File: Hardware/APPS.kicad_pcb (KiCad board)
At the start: 2 copper layers, 104.1 x 63 mm, 86 parts, among them J1 Screw_Terminal_01x02, J2 Screw_Terminal_01x03, J3 Screw_Terminal_01x03, J4 Conn_01x06_Male, J5 Screw_Terminal_01x02, J6 Conn_01x06_Male, J7 Screw_Terminal_01x02, K1 FINDER-30.22, Q1 BSS138, SW1 SW_Push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

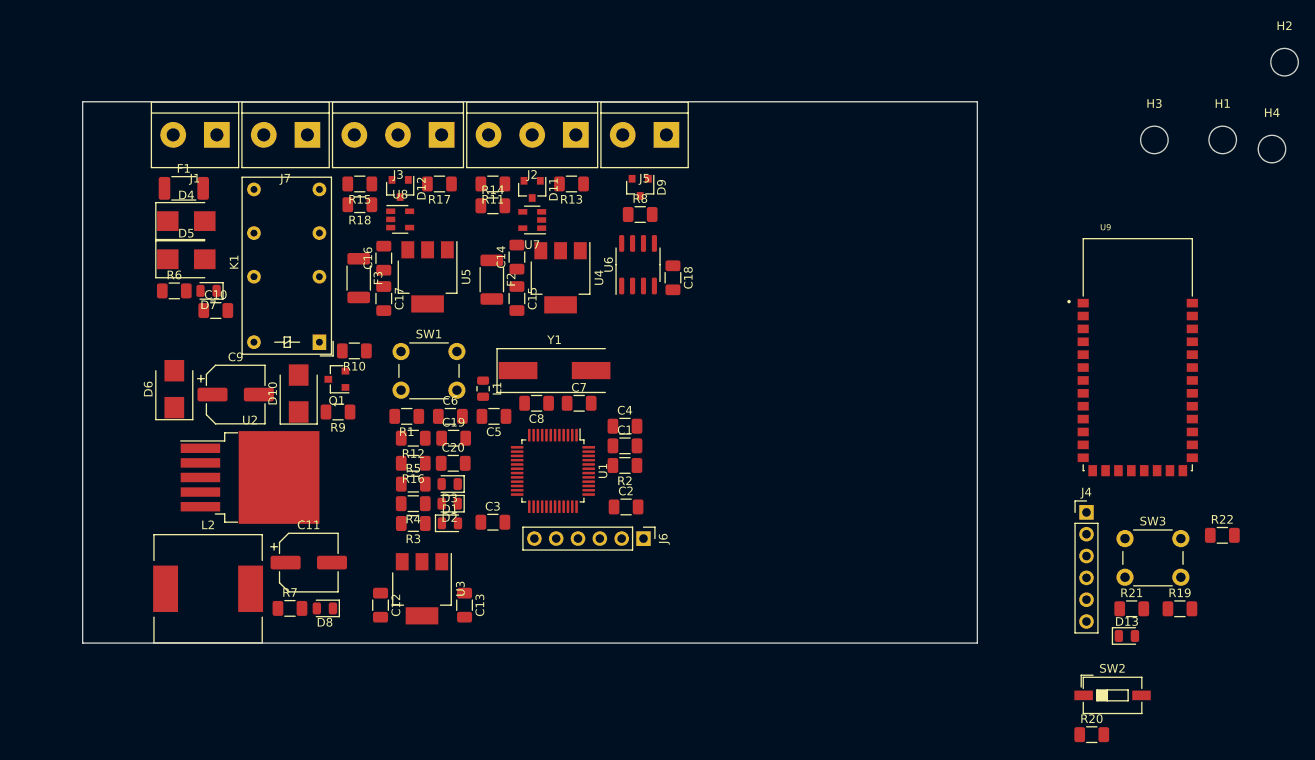
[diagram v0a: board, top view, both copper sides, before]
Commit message: Changed PCB edhes shape
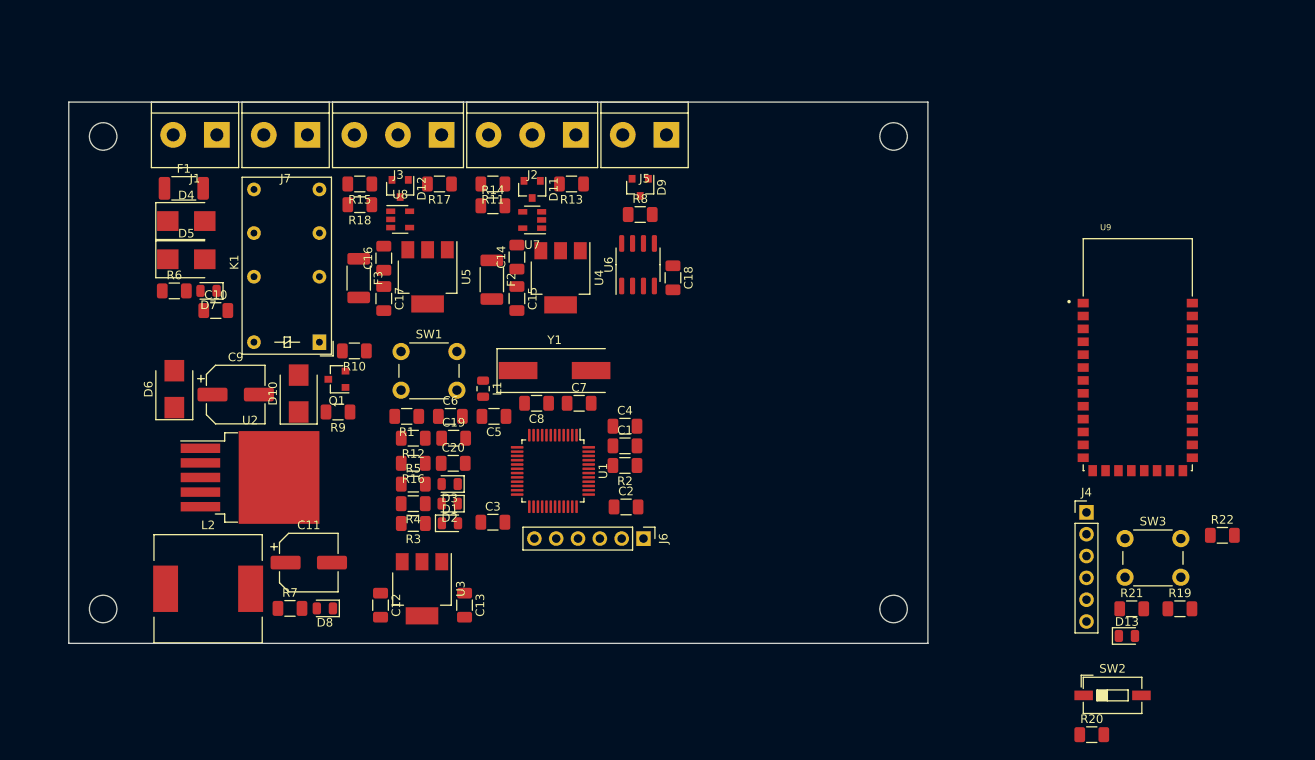
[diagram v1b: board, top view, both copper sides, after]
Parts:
- removed H1, H2, H3, H4: MountingHole, MountingHole:MountingHole_3.2mm_M3
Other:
- board size 104.1 x 63 mm -> 100 x 63 mm
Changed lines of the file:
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@@
   (general
     (thickness 1.6)
-    (drawings 4)
+    (drawings 8)
     (tracks 0)
     (zones 0)
-    (modules 86)
+    (modules 82)
     (nets 108)
   )
@@
     (solder_mask_min_width 0.25)
     (aux_axis_origin 0 0)
-    (visible_elements FFFFFF7F)
+    (visible_elements 7FFFFFFF)
     (pcbplotparams
       (layerselection 0x010fc_ffffffff)
@@
     )
   )
-  (module MountingHole:MountingHole_3.2mm_M3 (layer F.Cu)
-    (at 206.354001 56.975001)
-    (descr "Mounting Hole 3.2mm, no annular, M3")
-    (tags "mounting hole 3.2mm no annular m3")
-    (attr virtual)
-    (fp_text reference H1 (at 0 -4.2) (layer F.SilkS)
-      (effects (font (size 1 1) (thickness 0.15)))
-    )
-    (fp_text value MountingHole (at 0 4.2) (layer F.Fab)
-      (effects (font (size 1 1) (thickness 0.15)))
-    )
-    (fp_text user %R (at 0.3 0) (layer F.Fab)
-      (effects (font (size 1 1) (thickness 0.15)))
-    )
-    (fp_circle (center 0 0) (end 3.2 0) (layer Cmts.User) (width 0.15))
-    (fp_circle (center 0 0) (end 3.45 0) (layer F.CrtYd) (width 0.05))
-    (pad 1 np_thru_hole circle (at 0 0) (size 3.2 3.2) (drill 3.2) (layers *.Cu *.Mask))
-  )
-  (module MountingHole:MountingHole_3.2mm_M3 (layer F.Cu)
-    (at 213.554001 47.925001)
-    (descr "Mounting Hole 3.2mm, no annular, M3")
-    (tags "mounting hole 3.2mm no annular m3")
-    (attr virtual)
-    (fp_text reference H2 (at 0 -4.2) (layer F.SilkS)
-      (effects (font (size 1 1) (thickness 0.15)))
-    )
-    (fp_text value MountingHole (at 0 4.2) (layer F.Fab)
-      (effects (font (size 1 1) (thickness 0.15)))
-    )
-    (fp_circle (center 0 0) (end 3.45 0) (layer F.CrtYd) (width 0.05))
-    (fp_circle (center 0 0) (end 3.2 0) (layer Cmts.User) (width 0.15))
-    (fp_text user %R (at 0.3 0) (layer F.Fab)
-      (effects (font (size 1 1) (thickness 0.15)))
-    )
-    (pad 1 np_thru_hole circle (at 0 0) (size 3.2 3.2) (drill 3.2) (layers *.Cu *.Mask))
-  )
-  (module MountingHole:MountingHole_3.2mm_M3 (layer F.Cu)
-    (at 198.404001 56.975001)
-    (descr "Mounting Hole 3.2mm, no annular, M3")
-    (tags "mounting hole 3.2mm no annular m3")
-    (attr virtual)
-    (fp_text reference H3 (at 0 -4.2) (layer F.SilkS)
-      (effects (font (size 1 1) (thickness 0.15)))
-    )
-    (fp_text value MountingHole (at 0 4.2) (layer F.Fab)
-      (effects (font (size 1 1) (thickness 0.15)))
-    )
-    (fp_circle (center 0 0) (end 3.45 0) (layer F.CrtYd) (width 0.05))
-    (fp_circle (center 0 0) (end 3.2 0) (layer Cmts.User) (width 0.15))
-    (fp_text user %R (at 0.3 0) (layer F.Fab)
-      (effects (font (size 1 1) (thickness 0.15)))
-    )
-    (pad 1 np_thru_hole circle (at 0 0) (size 3.2 3.2) (drill 3.2) (layers *.Cu *.Mask))
-  )
-  (module MountingHole:MountingHole_3.2mm_M3 (layer F.Cu)
-    (at 212.09 58.039)
-    (descr "Mounting Hole 3.2mm, no annular, M3")
-    (tags "mounting hole 3.2mm no annular m3")
-    (attr virtual)
-    (fp_text reference H4 (at 0 -4.2) (layer F.SilkS)
-      (effects (font (size 1 1) (thickness 0.15)))
-    )
-    (fp_text value MountingHole (at 0 4.2) (layer F.Fab)
-      (effects (font (size 1 1) (thickness 0.15)))
-    )
-    (fp_text user %R (at 0.3 0) (layer F.Fab)
-      (effects (font (size 1 1) (thickness 0.15)))
-    )
-    (fp_circle (center 0 0) (end 3.2 0) (layer Cmts.User) (width 0.15))
-    (fp_circle (center 0 0) (end 3.45 0) (layer F.CrtYd) (width 0.05))
-    (pad 1 np_thru_hole circle (at 0 0) (size 3.2 3.2) (drill 3.2) (layers *.Cu *.Mask))
-  )
   (module TerminalBlock:TerminalBlock_bornier-2_P5.08mm (layer F.Cu)
     (at 89.281 56.388 180)
@@
     )
   )
-  (gr_line (start 73.66 115.54) (end 73.66 52.54) (layer Edge.Cuts) (width 0.05))
-  (gr_line (start 177.8 115.54) (end 73.66 115.54) (layer Edge.Cuts) (width 0.05))
-  (gr_line (start 177.8 52.54) (end 73.66 52.54) (layer Edge.Cuts) (width 0.05))
-  (gr_line (start 177.8 115.54) (end 177.8 52.54) (layer Edge.Cuts) (width 0.05))
+  (gr_line (start 172.046008 115.573201) (end 172.046008 52.573201) (layer Edge.Cuts) (width 0.1))
+  (gr_circle (center 168.046008 56.573201) (end 169.646008 56.573201) (layer Edge.Cuts) (width 0.1))
+  (gr_line (start 72.046008 115.573201) (end 172.046008 115.573201) (layer Edge.Cuts) (width 0.1))
+  (gr_circle (center 76.046008 111.573201) (end 77.646008 111.573201) (layer Edge.Cuts) (width 0.1))
+  (gr_line (start 72.046008 52.573201) (end 72.046008 115.573201) (layer Edge.Cuts) (width 0.1))
+  (gr_line (start 172.046008 52.573201) (end 72.046008 52.573201) (layer Edge.Cuts) (width 0.1))
+  (gr_circle (center 168.046008 111.573201) (end 169.646008 111.573201) (layer Edge.Cuts) (width 0.1))
+  (gr_circle (center 76.046008 56.573201) (end 77.646008 56.573201) (layer Edge.Cuts) (width 0.1))
 )

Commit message: Positioned Bluetooth module
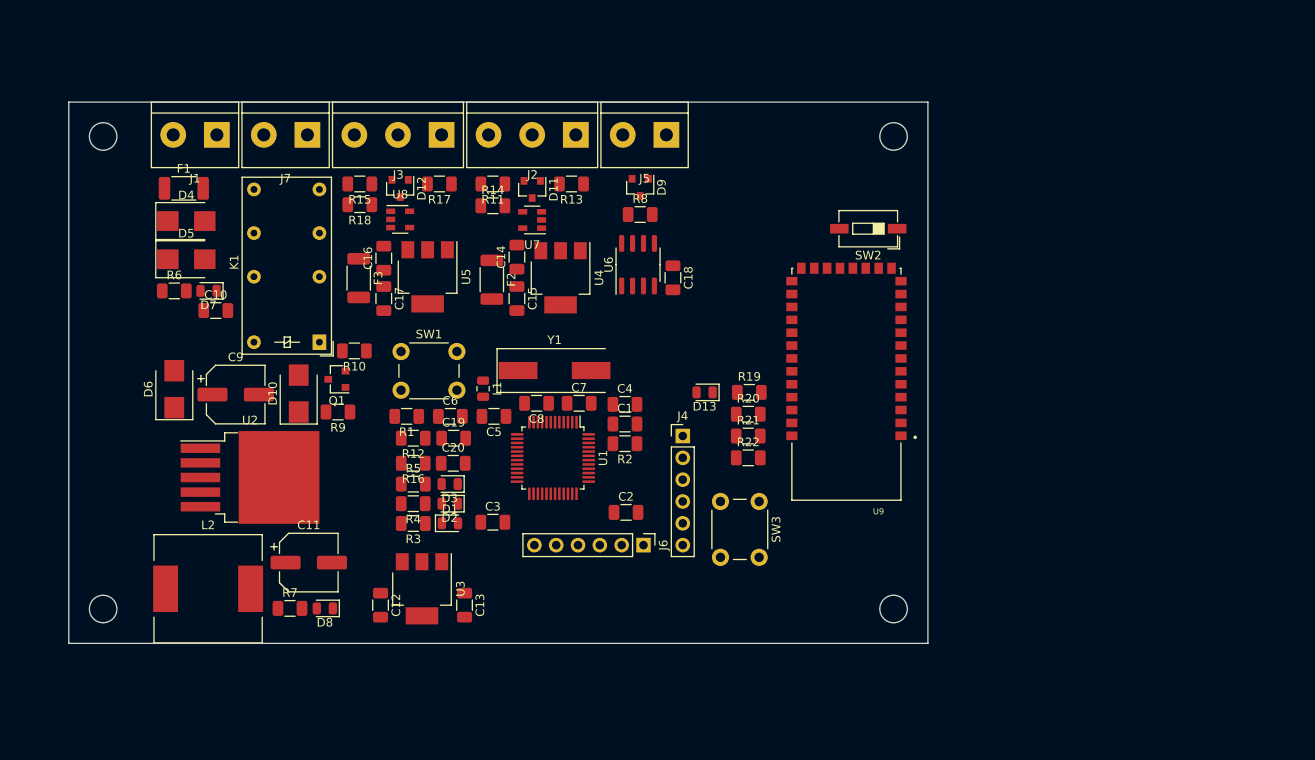
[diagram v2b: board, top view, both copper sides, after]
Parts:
- moved SW2 61.3 mm to (165.1, 67.3), turned to 180 degrees
- moved D13 56.7 mm to (146.1, 86.4), turned to 180 degrees
- moved R19 56.1 mm to (151.3, 86.4)
- moved R22 55.9 mm to (151.1, 94.0)
- moved R20 54.7 mm to (151.1, 88.9)
- moved R21 49.0 mm to (151.1, 91.4)
- moved J4 47.8 mm to (143.5, 91.4)
- moved SW3 42.8 mm to (152.4, 99.1), turned to 270 degrees
- moved U9 34.0 mm to (162.6, 85.1), turned to 180 degrees
- moved R2 2.54 mm to (136.8, 92.3)
- moved C1 2.54 mm to (136.8, 90.0)
- moved C4 2.54 mm to (136.8, 87.8)
- moved U1 1.50 mm to (128.4, 94.0)
- moved J6 0.76 mm to (138.9, 104.1)
- moved C2 0.64 mm to (136.9, 100.3)
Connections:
- U1 pad 13: BT_KEY -> Net-(U1-Pad13)
- U1 pad 14: BT_LED -> Net-(U1-Pad14)
- U1 pad 30: BT_TX -> Net-(U1-Pad30)
- U1 pad 31: BT_RX -> Net-(U1-Pad31)
- U1 pad 40: Net-(U1-Pad40) -> BT_KEY
- U1 pad 41: Net-(U1-Pad41) -> BT_LED
- U1 pad 42: Net-(U1-Pad42) -> BT_TX
- U1 pad 43: Net-(U1-Pad43) -> BT_RX

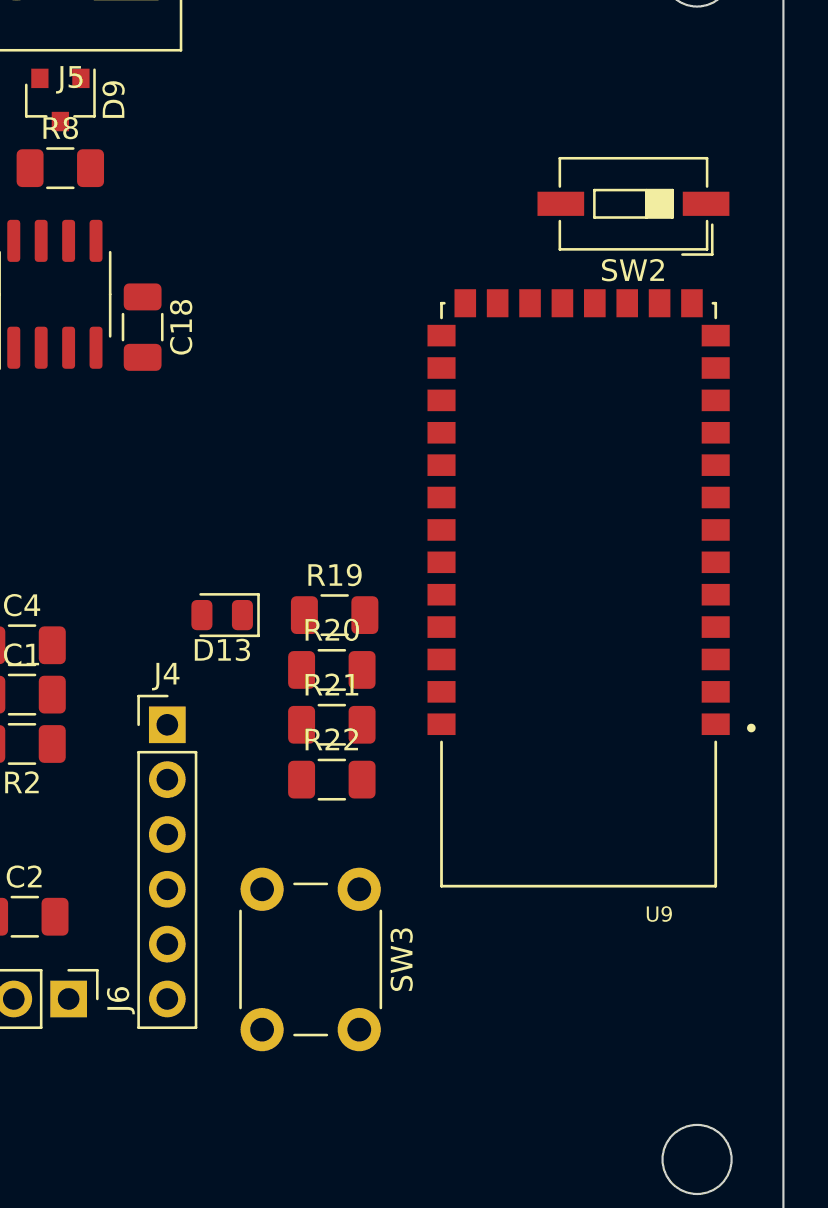
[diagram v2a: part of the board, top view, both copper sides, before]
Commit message: Updated BT position
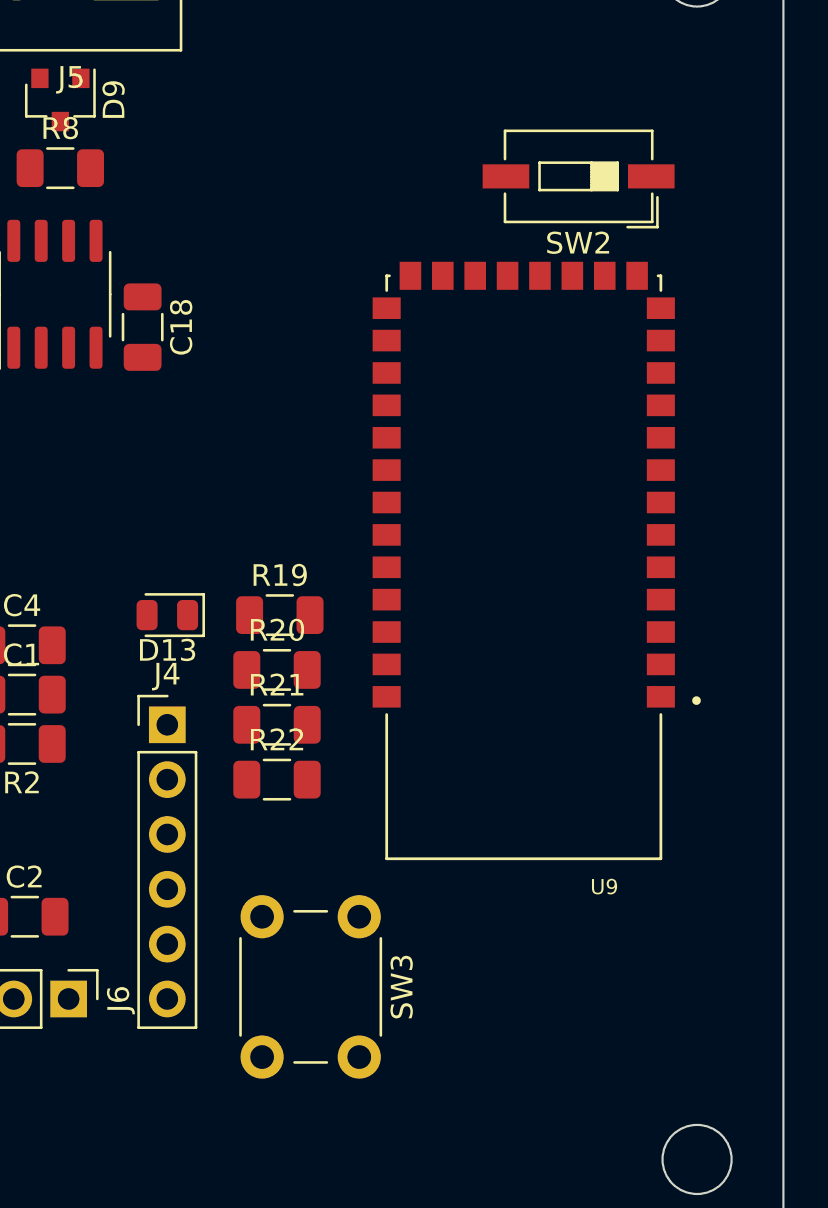
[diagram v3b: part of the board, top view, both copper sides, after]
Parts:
- moved U9 2.84 mm to (160.0, 83.8)
- moved SW2 2.84 mm to (162.6, 66.0)
- moved D13 2.54 mm to (143.5, 86.4)
- moved R19 2.54 mm to (148.7, 86.4)
- moved R20 2.54 mm to (148.6, 88.9)
- moved R21 2.54 mm to (148.6, 91.4)
- moved R22 2.54 mm to (148.6, 94.0)
- moved SW3 1.27 mm to (152.4, 100.3)

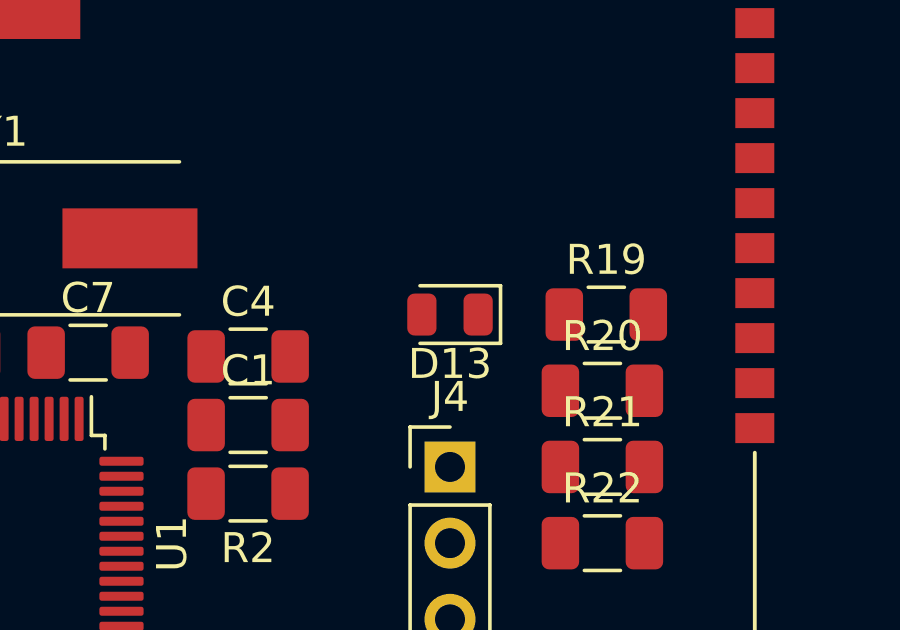
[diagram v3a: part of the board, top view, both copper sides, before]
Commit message: Updated BT position
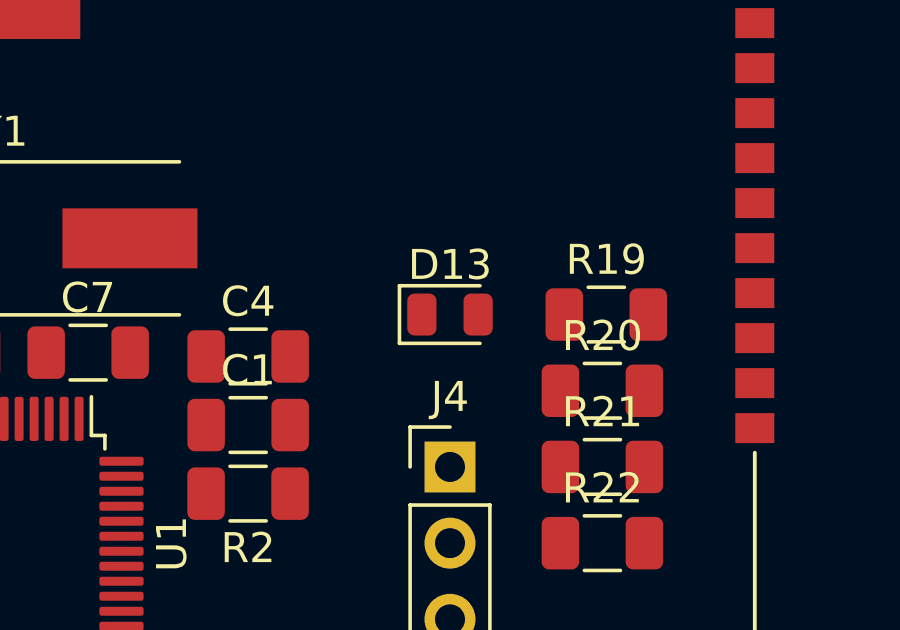
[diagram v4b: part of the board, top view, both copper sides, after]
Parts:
- turned D13 to 0 degrees

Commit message: Changed HC-05 pins for other Forbot HC-05
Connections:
- J4 pad 2: BT_KEY -> BT_RX
- J4 pad 3: BT_RX -> BT_TX
- J4 pad 4: BT_TX -> SW_GND
- J4 pad 5: SW_GND -> 3V3_SYS
- J4 pad 6: 3V3_SYS -> BT_KEY
- U1 pad 41: BT_LED -> Net-(U1-Pad41)
- U1 pad 46: Net-(U1-Pad46) -> BT_LED

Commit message: Quick fixes
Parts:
- moved SW2 49.4 mm to (141.0, 110.5)
- moved D13 27.9 mm to (168.3, 99.0), turned to 180 degrees
- moved SW3 24.1 mm to (144.8, 77.5)
- moved R19 19.7 mm to (163.8, 99.1), turned to 180 degrees
- moved U9 17.7 mm to (153.7, 100.3), turned to 0 degrees
- moved R20 17.0 mm to (163.8, 96.5), turned to 180 degrees
- moved R21 15.5 mm to (163.8, 94.0), turned to 180 degrees
- moved R22 15.5 mm to (163.8, 91.4), turned to 180 degrees
- moved J4 10.2 mm to (143.5, 101.6), turned to 180 degrees
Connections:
- U1 pad 40: BT_KEY -> BT_LED
- U1 pad 42: BT_TX -> BT_RX
- U1 pad 43: BT_RX -> BT_TX
- U1 pad 46: BT_LED -> BT_KEY

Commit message: PCB router 50%
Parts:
- added JP1: Jumper_NC_Small, Connector_PinHeader_2.54mm:PinHeader_1x02_P2.54mm_Vertical, F.Cu at (135.8, 62.7)
- moved R21 30.5 mm to (166.4, 63.6)
- moved R20 30.5 mm to (166.4, 66.2)
- moved R22 30.5 mm to (166.4, 61.1)
- moved U9 30.5 mm to (156.2, 70.0)
- moved R19 27.9 mm to (165.9, 71.2), turned to 90 degrees
- moved SW2 25.9 mm to (153.7, 87.9), turned to 0 degrees
- moved D13 23.2 mm to (165.9, 75.9), turned to 90 degrees
- moved D9 1.52 mm to (140.1, 62.5)
- moved R8 1.52 mm to (140.1, 65.7)
- turned D11 to 90 degrees
- turned D12 to 90 degrees
- turned R11 to 0 degrees
- turned R13 to 0 degrees
- turned R15 to 0 degrees
- turned R17 to 0 degrees
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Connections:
- D11 pad 1: Net-(D11-Pad1) -> 3V3_POT1
- R8 pad 1: CAN_H -> Net-(JP1-Pad2)
- U7 pad 5: Net-(U7-Pad5) -> 3V3_POT1
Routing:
- net 3V3_SYS: track 0.00 -> 145.6 mm, vias 0 -> 9
- net +5V: track 0.00 -> 111.6 mm, vias 0 -> 7
- net +24V: track 0.00 -> 35.7 mm
- net 3V3_POT2: track 0.00 -> 19.5 mm
- net 3V3_POT1: track 0.00 -> 19.4 mm
- net CAN_H: track 0.00 -> 18.8 mm
- net Net-(C17-Pad1): track 0.00 -> 16.9 mm
- net SW_GND: track 0.00 -> 15.8 mm
- net Net-(D10-Pad1): track 0.00 -> 15.5 mm
- net Net-(C15-Pad1): track 0.00 -> 15.0 mm
- net CAN_L: track 0.00 -> 14.1 mm
- net Net-(D12-Pad3): track 0.00 -> 9.57 mm
- net Net-(D11-Pad3): track 0.00 -> 9.53 mm
- net Net-(Q1-Pad1): track 0.00 -> 8.37 mm
- net Net-(R12-Pad2): track 0.00 -> 8.15 mm
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- added copper zone on F.Cu, net +5V
- added copper zone on F.Cu, net Net-(D6-Pad1)
- added copper zone on B.Cu, net SW_GND
- added copper zone on F.Cu, net SW_GND
